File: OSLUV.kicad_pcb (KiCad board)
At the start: 4 copper layers, 110 x 90 mm, 190 parts, among them IC1 NCP12510ASN65T1G, IC2 SFH6156-3, IC3 INA210, IC4 AP63300WU-7, IC5 AP63300WU-7, IC6 STM32G071KBT6, IC7 TLV9001IDBVR, IC8 FAN3100TSX, IC9 TLV1821, J1 B08B-XASK-1-A_LF__SN_, J2 TC2050-IDC, J3 BM02B-SRSS-TB_LF__SN_, J4 BM02B-SRSS-TB_LF__SN_, J5 640445-2, J6 640445-2, J7 B5P-VH, Q1 STD3NK80ZT4, Q2 BAT847B, Q3 BSS138, Q4 BC807, T1 750343466, T4 NMOS_GDS-KS_SMD, U1 OPA2356AIDGKR, U2 AZ431LANTR

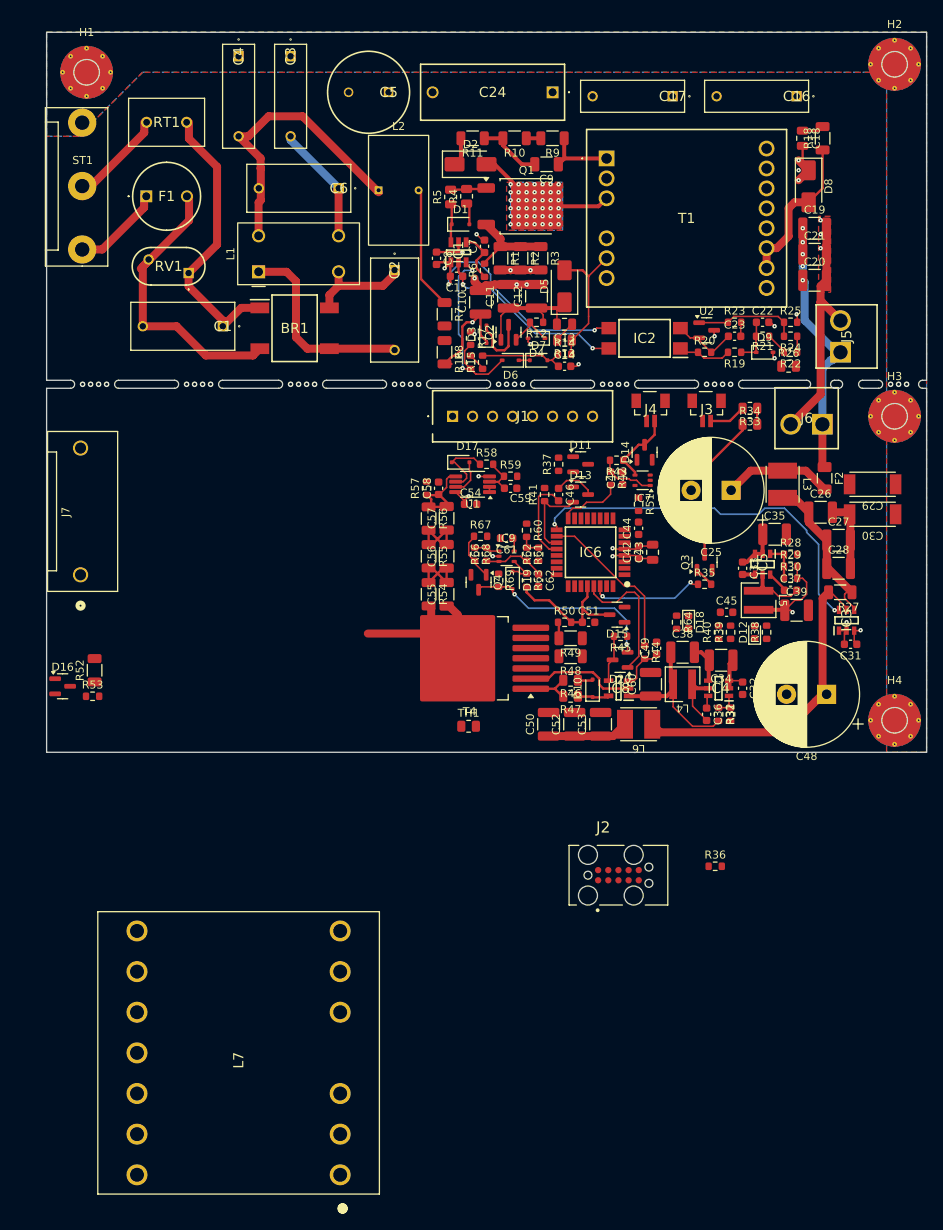
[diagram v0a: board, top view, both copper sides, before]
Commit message: branch main, transfomer changed to EF25
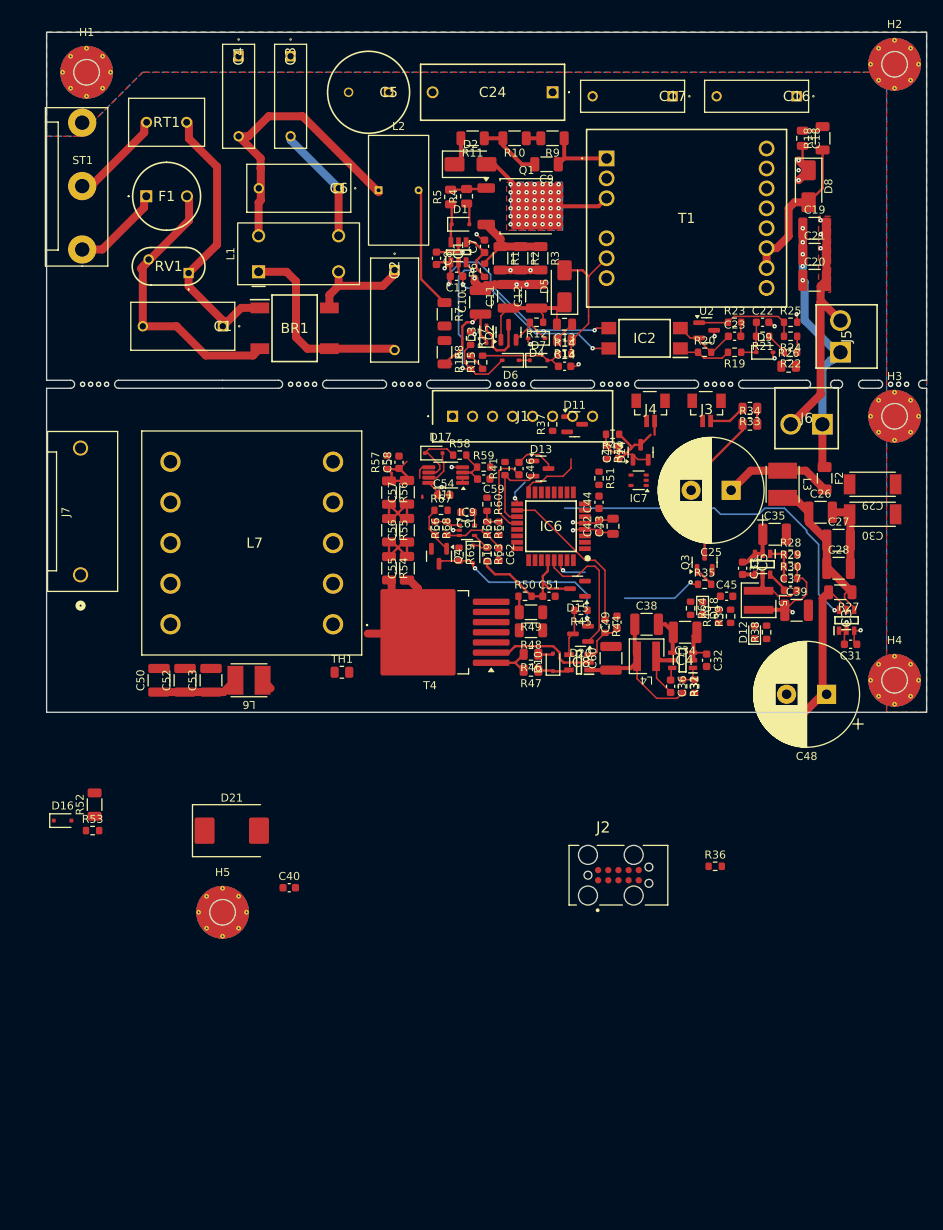
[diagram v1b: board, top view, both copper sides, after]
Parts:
- added C40: 47n 0603, Capacitor_SMD:C_0603_1608Metric, F.Cu at (80.3, 156.9)
- added D21: 3KASMC24AHE3, Diode_SMD:D_SMC, F.Cu at (73.1, 149.8)
- added H5: MountingHole_Pad, Hansmann:Mounting_M3_NPTH_Vias, F.Cu at (72.0, 160.0)
- D16: value BAS40-04 -> BAT54J; footprint Package_TO_SOT_SMD:SOT-23 -> Diode_SMD:D_SOD-323F
- L7: value ETD29 -> EF25; footprint Hansmann:B66359B1013T001 -> Hansmann:B66208B1110T1
- R52: value 1R 1206 -> 82R 1206/MMA
- R53: value 1k 0603 -> 51R 0603
- moved L7 54.9 mm to (85.8, 124.0), turned to 180 degrees
- moved C50 49.0 mm to (64.0, 131.0)
- moved C52 49.0 mm to (67.3, 131.0)
- moved C53 49.0 mm to (70.5, 131.0)
- moved L6 49.0 mm to (75.3, 131.0)
- moved TH1 17.2 mm to (86.9, 130.0)
- moved D16 16.8 mm to (52.0, 148.5)
- moved R52 16.8 mm to (56.0, 146.5)
- moved R53 16.8 mm to (55.8, 149.8)
- moved C42 5.92 mm to (119.0, 111.8)
- moved C43 5.92 mm to (120.8, 111.8)
- moved C44 5.92 mm to (119.0, 108.8)
- moved C46 5.92 mm to (109.0, 104.5)
- moved C49 5.92 mm to (121.3, 123.8)
- moved C51 5.92 mm to (112.8, 120.5)
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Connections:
- C50 pad 1: /excimerDriver/lampDriver/VDC_Trafo -> /excimerDriver/VDC_power
- C52 pad 1: /excimerDriver/lampDriver/VDC_Trafo -> /excimerDriver/VDC_power
- C53 pad 1: /excimerDriver/lampDriver/VDC_Trafo -> /excimerDriver/VDC_power
- D16 pad 1: GND -> Net-(D16-K)
- D16 pad 2: +3V3 -> Net-(D16-A)
- L6 pad 2: /excimerDriver/lampDriver/VDC_Trafo -> /excimerDriver/VDC_power
- L7 pad 1: unconnected-(L7-Pad1) -> /excimerDriver/lampDriver/HV_Drain
- L7 pad 10: unconnected-(L7-Pad10) -> /excimerDriver/VDC_power
- L7 pad 2: /excimerDriver/lampDriver/HV_Drain -> unconnected-(L7-Pad2)
- L7 pad 4: unconnected-(L7-Pad4) -> (no net)
- L7 pad 5: Net-(L7-Pad5) -> GND
- L7 pad 6: Net-(L7-Pad5) -> /excimerDriver/lampDriver/Lamp_HV
- L7 pad 7: unconnected-(L7-Pad7) -> (no net)
- L7 pad 8: /excimerDriver/lampDriver/Lamp_HV -> unconnected-(L7-Pad8)
- R53 pad 1: Net-(D16-Pad3) -> Net-(D16-A)
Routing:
- net /excimerDriver/lampDriver/VDC_Trafo: track 10.2 -> 0.00 mm
- net /excimerDriver/VDC_power: track 40.1 -> 34.7 mm
- net unconnected-(L7-Pad9): vias 0 -> 3
- net (no net): vias 28 -> 21
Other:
- board size 110 x 90 mm -> 110 x 85 mm

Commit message: new transformer, top layer only
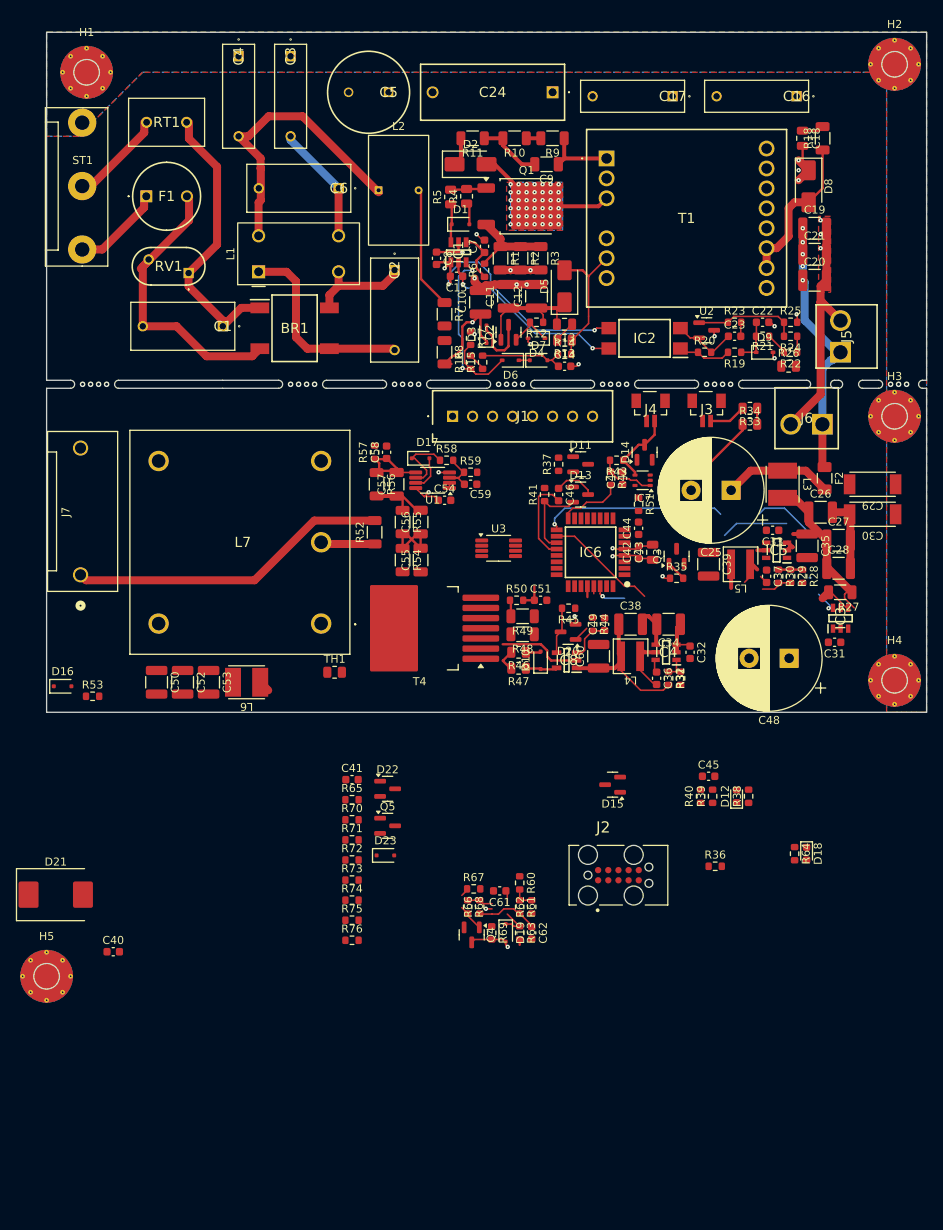
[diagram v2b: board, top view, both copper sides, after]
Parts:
- removed IC9: TLV1821, Package_TO_SOT_SMD:SOT-353_SC-70-5
- added C41: 100n 0603, Capacitor_SMD:C_0603_1608Metric, F.Cu at (88.2, 143.4)
- added D22: BAS40-04, Package_TO_SOT_SMD:SOT-23, F.Cu at (92.6, 144.6)
- added D23: BAT54J, Diode_SMD:D_SOD-323F, F.Cu at (92.3, 152.9)
- added Q5: BC807, Package_TO_SOT_SMD:SOT-23, F.Cu at (92.6, 149.2)
- added R65: 10k 0603, Resistor_SMD:R_0603_1608Metric, F.Cu at (88.2, 145.9)
- added R70: 10k 0603, Resistor_SMD:R_0603_1608Metric, F.Cu at (88.2, 148.4)
- added R71: 2k2 0603, Resistor_SMD:R_0603_1608Metric, F.Cu at (88.2, 150.9)
- added R72: 1k 0603, Resistor_SMD:R_0603_1608Metric, F.Cu at (88.2, 153.5)
- added R73: 10k 0603, Resistor_SMD:R_0603_1608Metric, F.Cu at (88.2, 156.0)
- added R74: 100k 0603, Resistor_SMD:R_0603_1608Metric, F.Cu at (88.2, 158.5)
- added R75: 10k 0603, Resistor_SMD:R_0603_1608Metric, F.Cu at (88.2, 161.0)
- added R76: 10k 0603, Resistor_SMD:R_0603_1608Metric, F.Cu at (88.2, 163.5)
- added U3: LM2904, Package_SO:VSSOP-8_3x3mm_P0.65mm, F.Cu at (106.5, 114.5)
- L7: footprint Hansmann:B66208B1110T1 -> OSLUV:EF25_outerPinsOnly
- T4: footprint Hansmann:TO-263-7_TabPin2 -> Hansmann:TO-263-7_TabPin2_HV
- moved R52 48.8 mm to (91.0, 112.5)
- moved C61 47.5 mm to (106.6, 157.3)
- moved C62 47.5 mm to (110.6, 162.6)
- moved D19 47.5 mm to (107.4, 162.6)
- moved Q4 47.5 mm to (103.1, 162.8)
- moved R60 47.5 mm to (109.1, 156.3)
- moved R61 47.5 mm to (109.1, 159.3)
- moved R62 47.5 mm to (110.6, 159.3)
- moved R63 47.5 mm to (109.1, 162.6)
- moved R66 47.5 mm to (104.1, 159.3)
- moved R67 47.5 mm to (103.4, 157.1)
- moved R68 47.5 mm to (102.6, 159.3)
- moved R69 47.5 mm to (105.6, 162.6)
- moved D18 33.3 mm to (145.0, 152.7)
- moved R64 33.3 mm to (143.5, 152.7)
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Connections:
- net Net-(D16-K) renamed /excimerDriver/Isense_Lamp
- C50 pad 1: /excimerDriver/VDC_power -> /excimerDriver/lampDriver/VDC_Trafo
- C52 pad 1: /excimerDriver/VDC_power -> /excimerDriver/lampDriver/VDC_Trafo
- C53 pad 1: /excimerDriver/VDC_power -> /excimerDriver/lampDriver/VDC_Trafo
- L6 pad 2: /excimerDriver/VDC_power -> /excimerDriver/lampDriver/VDC_Trafo
- L7 pad 10: /excimerDriver/VDC_power -> /excimerDriver/lampDriver/VDC_Trafo
- L7 pad 3: unconnected-(L7-Pad3) -> GND
- L7 pad 5: GND -> unconnected-(L7-Pad5)
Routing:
- net /excimerDriver/lampDriver/Lamp_GND: track 0.00 -> 40.1 mm
- net /excimerDriver/VDC_power: track 34.7 -> 5.79 mm
- net /excimerDriver/lampDriver/HV_Drain: track 26.7 -> 0.00 mm
- net Net-(D19-A): track 24.7 -> 6.32 mm
- net /excimerDriver/DRV_Mask: track 17.2 -> 2.91 mm
- net /excimerDriver/Isense_MOS: track 17.7 -> 5.19 mm
- net +3V3: track 34.5 -> 24.3 mm, vias 4 -> 2
- net /excimerDriver/UV_LED: track 14.3 -> 5.27 mm
- net /excimerDriver/DRV: track 20.3 -> 14.1 mm
- net Net-(Q3-D): track 18.3 -> 12.7 mm
- net /excimerDriver/Isense_In: track 47.4 -> 42.6 mm
- net Net-(D21-K): track 13.7 -> 16.9 mm
- net Net-(T4-G): track 6.54 -> 3.54 mm
- net Net-(IC5-BST): track 2.69 -> 0.18 mm
- net Net-(C56-Pad2): track 9.58 -> 7.72 mm
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
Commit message: routing single side done
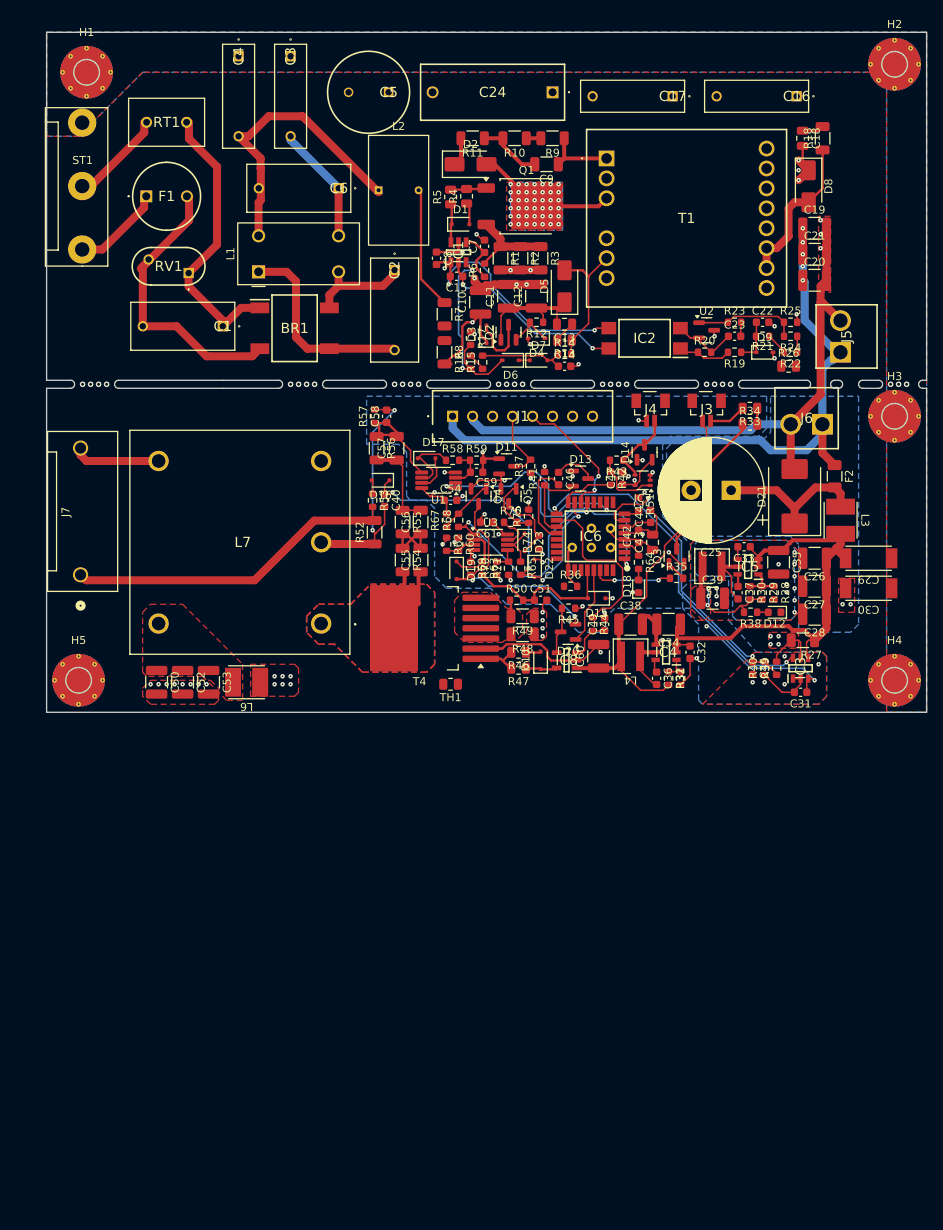
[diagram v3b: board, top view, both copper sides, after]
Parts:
- removed C41, C62: 100n 0603, Capacitor_SMD:C_0603_1608Metric
- removed C48: 330u 35V, Capacitor_THT:CP_Radial_D13.0mm_P5.00mm
- removed J2: TC2050-IDC, Hansmann:TAG-CONNECT_TC2050-IDC
- removed R61, R72: 1k 0603, Resistor_SMD:R_0603_1608Metric
- removed R66, R73: 10k 0603, Resistor_SMD:R_0603_1608Metric
- added U4: Prog, Hansmann:Prog_St, B.Cu at (120.5, 114.4)
- D15, D22: value BAS40-04 -> BAT54J; footprint Package_TO_SOT_SMD:SOT-23 -> Diode_SMD:D_SOD-323F
- moved D21 104.9 mm to (143.5, 108.0), turned to 90 degrees
- moved C40 65.8 mm to (92.2, 108.5), turned to -90 degrees
- moved R76 55.9 mm to (108.0, 111.2)
- moved R75 55.1 mm to (110.2, 110.5), turned to 90 degrees
- moved Q4 54.8 mm to (104.0, 108.0)
- moved R74 50.4 mm to (111.5, 113.8), turned to 90 degrees
- moved R68 48.3 mm to (101.5, 111.0), turned to 90 degrees
- moved D16 47.4 mm to (91.8, 106.0), turned to 180 degrees
- moved R62 46.6 mm to (100.0, 114.0), turned to -90 degrees
- moved R67 46.2 mm to (100.0, 111.0), turned to 90 degrees
- moved C61 46.1 mm to (105.0, 111.2)
- moved R63 45.8 mm to (104.5, 117.0)
- moved D19 45.7 mm to (101.2, 117.2)
- moved R69 45.7 mm to (103.0, 117.0)
- moved Q5 43.9 mm to (107.8, 108.0), turned to -90 degrees
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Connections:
- net Net-(C56-Pad2) renamed /excimerDriver/lampDriver/HV_Drain_div2
- net Net-(R48-Pad2) renamed /excimerDriver/lampDriver/Source
- net Net-(U1B-+) renamed /excimerDriver/lampDriver/HV_Drain_div3
- C55 pad 2: Net-(C55-Pad2) -> /excimerDriver/lampDriver/HV_Drain_div
- C56 pad 1: Net-(C55-Pad2) -> /excimerDriver/lampDriver/HV_Drain_div
- D15 pad 1: GND -> +3V3
- D15 pad 2: +3V3 -> /excimerDriver/Isense_MOS
- D22 pad 1: GND -> +3V3
- D22 pad 2: +3V3 -> /excimerDriver/Isense_Lamp
- IC6 pad 15: /excimerDriver/IsenseLamp -> /excimerDriver/Isense_Lamp
- IC6 pad 24: /excimerDriver/SWDIO -> unconnected-(IC6-PA13-Pad24)
- R36 pad 2: /excimerDriver/SWCLK -> unconnected-(R36-Pad2)
- R54 pad 1: Net-(C55-Pad2) -> Net-(R54-Pad1)
- R55 pad 2: Net-(C55-Pad2) -> Net-(R54-Pad1)
- R60 pad 2: Net-(R60-Pad2) -> Net-(U3A-+)
- R62 pad 2: Net-(R60-Pad2) -> Net-(U3A-+)
- R70 pad 2: Net-(R70-Pad2) -> Net-(U3B-+)
- R71 pad 2: Net-(R70-Pad2) -> Net-(U3B-+)
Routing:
- net GND: track 105.1 -> 217.3 mm, vias 10 -> 62
- net /excimerDriver/VDC: track 71.2 -> 122.4 mm
- net +3V3: track 24.3 -> 73.1 mm, vias 2 -> 15
- net /excimerDriver/Isense_Lamp: track 0.00 -> 43.6 mm, vias 0 -> 4
- net /excimerDriver/24V_Sense: track 0.00 -> 37.3 mm, vias 0 -> 2
- net +15V: track 19.7 -> 49.9 mm
- net /excimerDriver/VDC_filter: track 28.8 -> 58.5 mm
- net /excimerDriver/Usense_Lamp: track 0.65 -> 28.3 mm, vias 0 -> 2
- net /excimerDriver/OCP: track 3.31 -> 28.3 mm, vias 0 -> 2
- net Net-(D19-A): track 6.32 -> 30.2 mm
- net /excimerDriver/MCU_REMOTE: track 0.00 -> 23.8 mm, vias 0 -> 2
- net /excimerDriver/Status: track 0.00 -> 16.8 mm, vias 0 -> 2
- net /excimerDriver/lampDriver/HV_Drain: track 0.00 -> 15.9 mm
- net /excimerDriver/Isense_MOS: track 5.19 -> 19.9 mm
- net /excimerDriver/lampDriver/Lamp_HV: track 0.00 -> 10.9 mm
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- added copper zone on F.Cu, net +3V3
- added copper zone on In2.Cu, net +3V3
- added copper zone on F.Cu, net /excimerDriver/VDC_power
- added copper zone on In2.Cu, net /excimerDriver/VDC_power
- added copper zone on B.Cu, net /excimerDriver/lampDriver/HV_Drain
- added copper zone on F.Cu, net /excimerDriver/lampDriver/HV_Drain
- added copper zone on In1.Cu, net /excimerDriver/lampDriver/HV_Drain
- added copper zone on In2.Cu, net /excimerDriver/lampDriver/HV_Drain
- added copper zone on F.Cu, net /excimerDriver/lampDriver/Source
- added copper zone on F.Cu, net /excimerDriver/lampDriver/VDC_Trafo
- added copper zone on B.Cu, net GND
